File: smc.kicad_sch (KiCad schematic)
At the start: 46 parts, among them SW1 SW_Push, SW2 SW_Push, U5 W25Q128JVS, U6 RP2040, Y1 12MHz 20pF

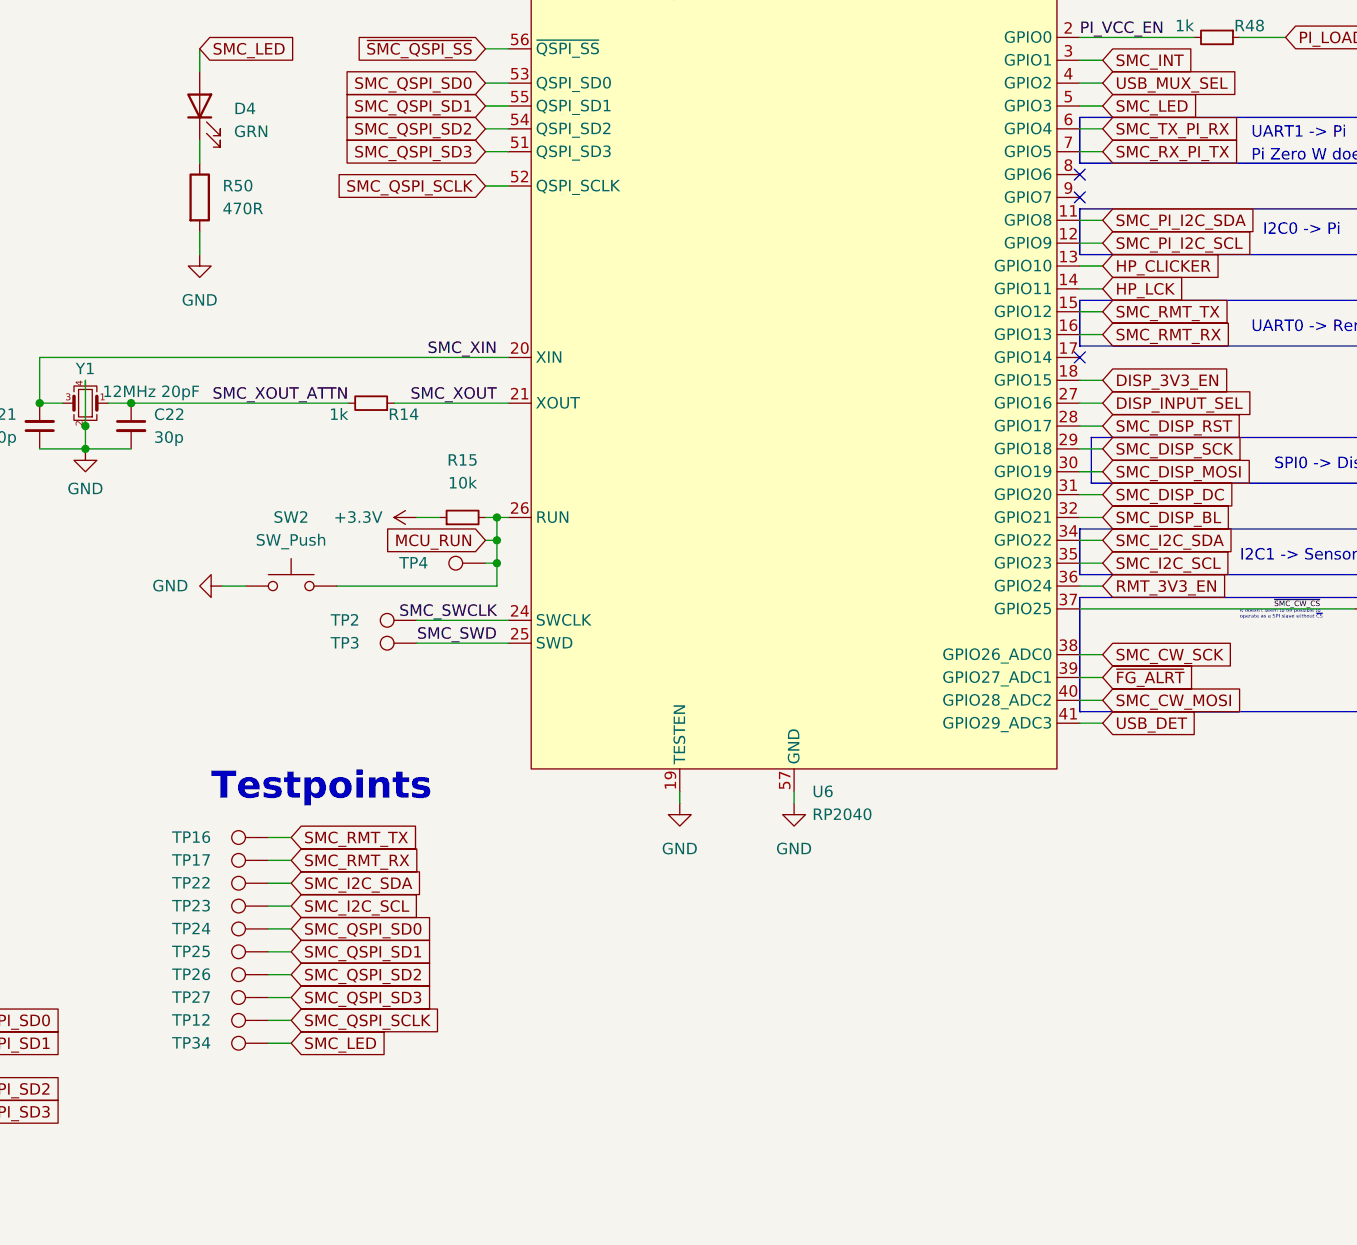
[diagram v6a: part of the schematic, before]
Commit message: feature: add hardware ID resistors
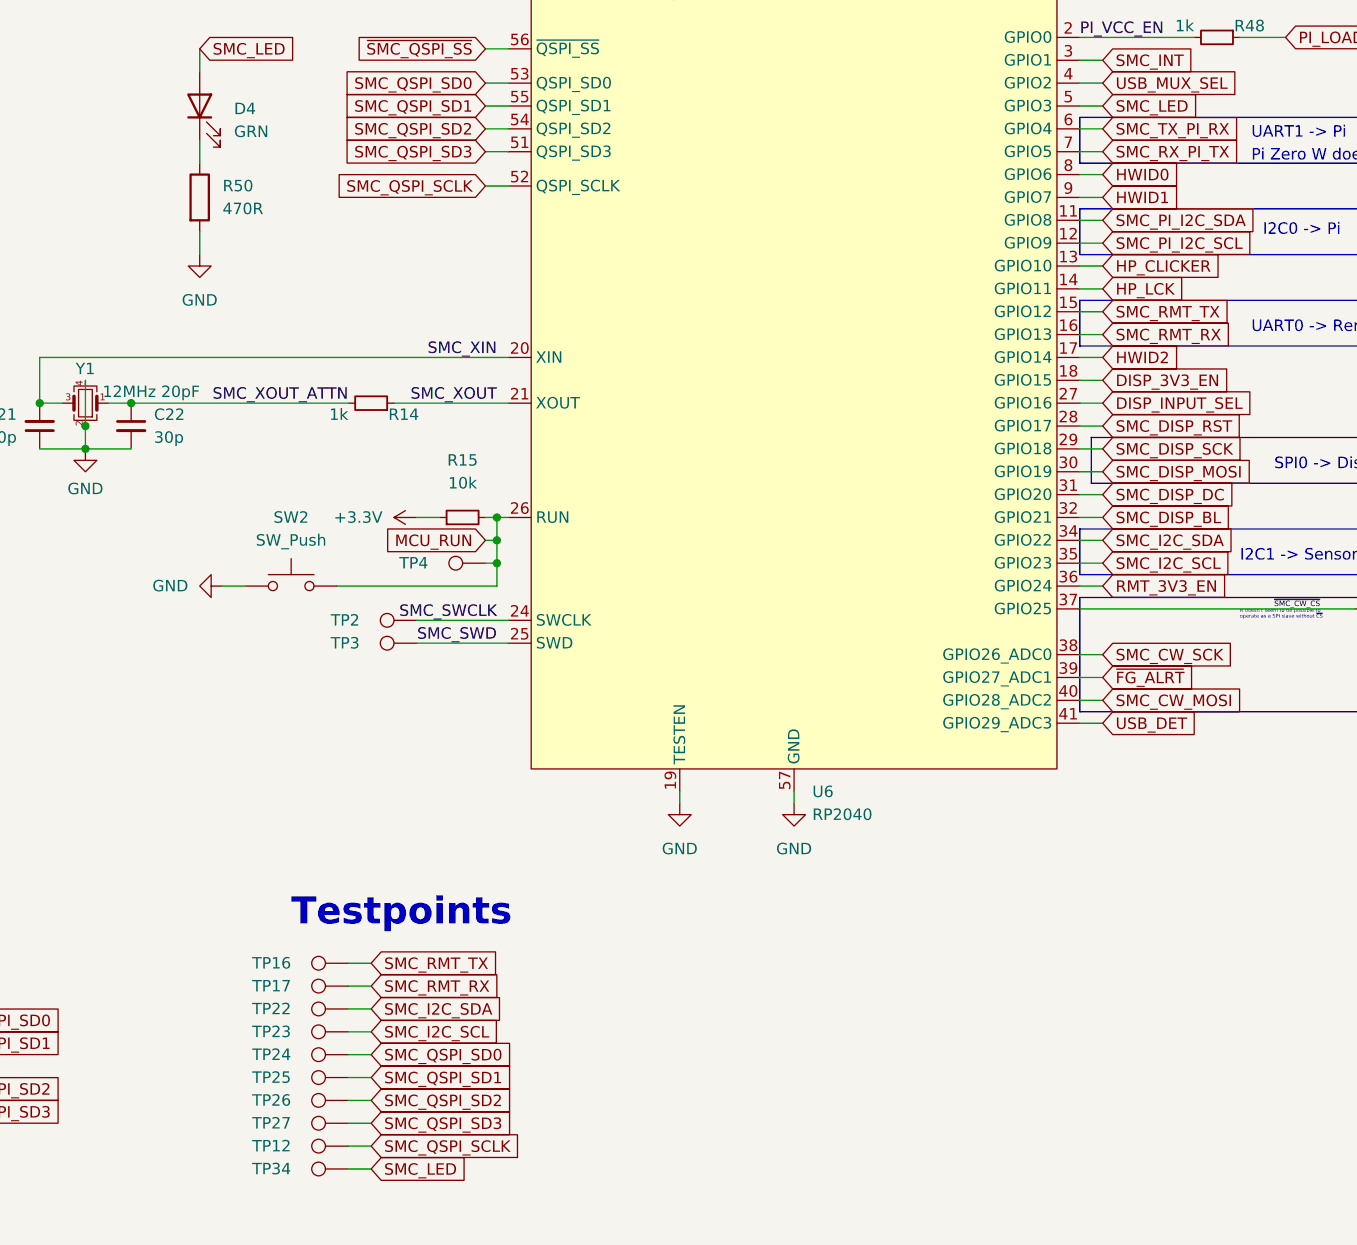
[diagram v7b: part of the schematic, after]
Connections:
- net HWID2: now reaches U6.17 (GPIO14)
- net HWID0: now reaches U6.8 (GPIO6)
- net HWID1: now reaches U6.9 (GPIO7)
- no-connect marks 3 -> 0
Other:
- moved on the sheet: TP12, TP16, TP17, TP22, TP23, TP24, TP25, TP26, TP27, TP34
